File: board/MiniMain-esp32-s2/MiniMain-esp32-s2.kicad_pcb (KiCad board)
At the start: 2 copper layers, 50.8 x 22.9 mm, 42 parts, among them IC1 ESP32-S2-MINI-1-N4R2, J1 USB4105-GF-A, J10 Conn_01x03_Male, J2 Conn_01x04, J3 Conn_01x16, J5 Conn_01x12, J8 Conn_01x02, Q1 DMP3130LQ-7, SW1 SW_Push, SW2 SW_Push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

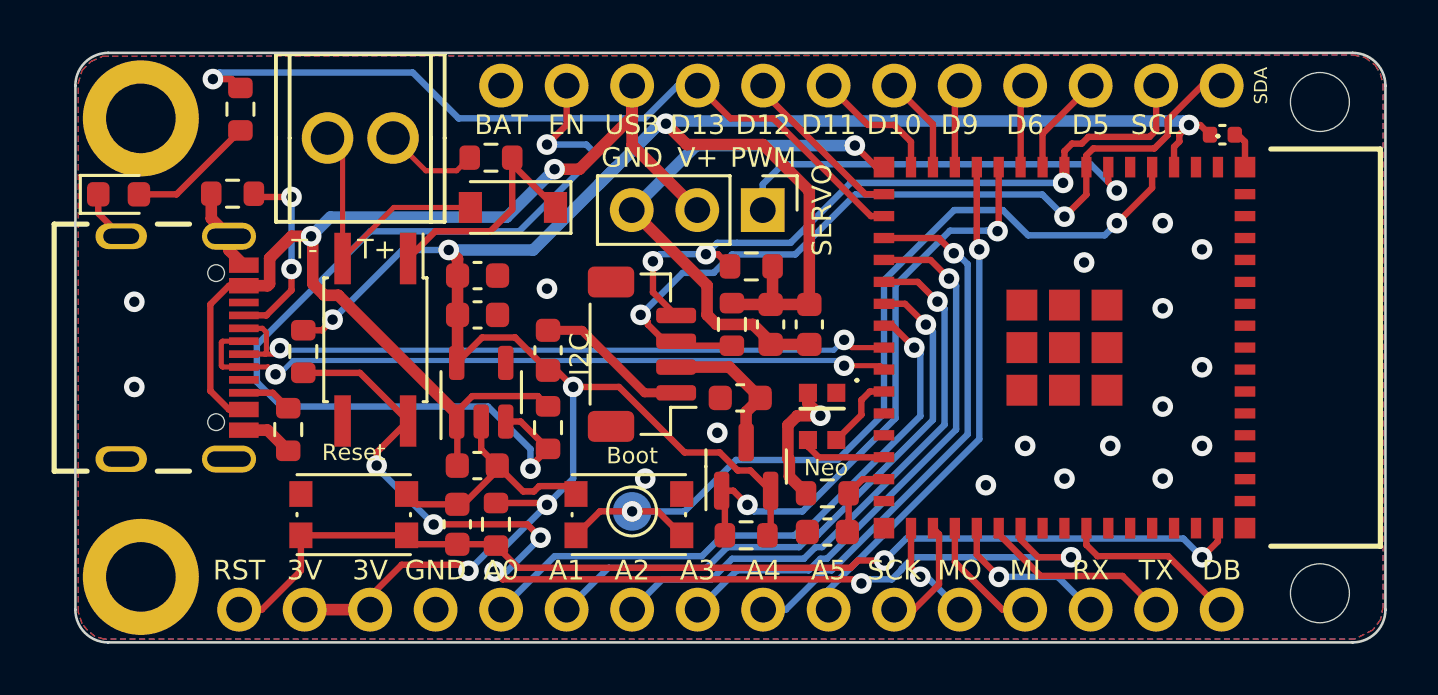
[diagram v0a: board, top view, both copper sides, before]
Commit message: Rev 2: Change Stemma QT compatible port from transistor controlled power to just +3.3V. Remove copper pour under the ESP32-S2 antenna. Perhaps look at changing the isolated input pull-up from 150 ohms to 1k ohms.
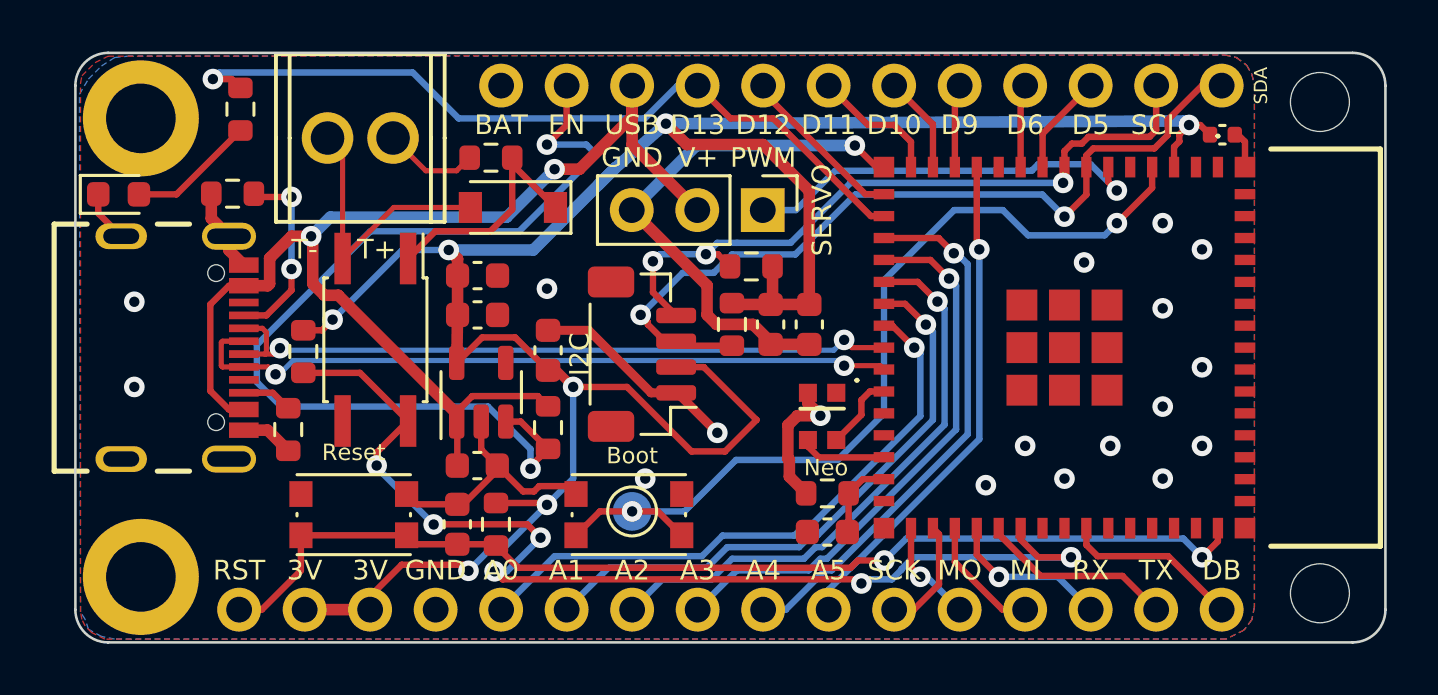
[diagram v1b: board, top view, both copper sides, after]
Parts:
- removed C5: 1uF, Capacitor_SMD:C_0603_1608Metric
- removed Q1: DMP3130LQ-7, Package_TO_SOT_SMD:SOT-23
- removed R9: 100k, Resistor_SMD:R_0603_1608Metric
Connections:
- IC1 pad 11: /I2C_PWR -> unconnected-(IC1-Pad11)
- J2 pad 2: /VDEVICE -> +3V3
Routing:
- net /I2C_PWR: track 22.9 -> 0.00 mm, vias 2 -> 0
- net /VDEVICE: track 5.70 -> 0.00 mm
- net GND: track 51.3 -> 53.5 mm
- net +3V3: track 97.2 -> 98.6 mm
- net /Servo1: track 16.5 -> 15.9 mm
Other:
- board text added: "Rev 2"
